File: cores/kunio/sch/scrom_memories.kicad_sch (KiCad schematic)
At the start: 18 parts

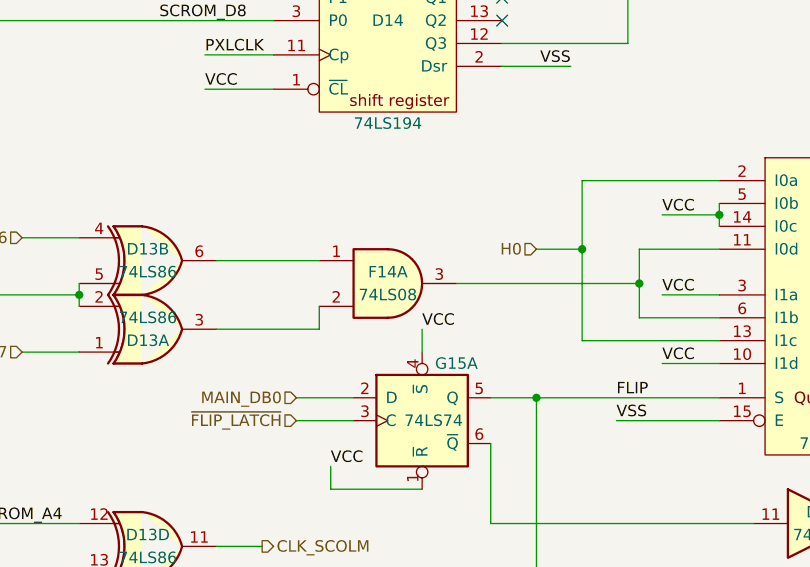
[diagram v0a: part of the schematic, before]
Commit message: update kicad7
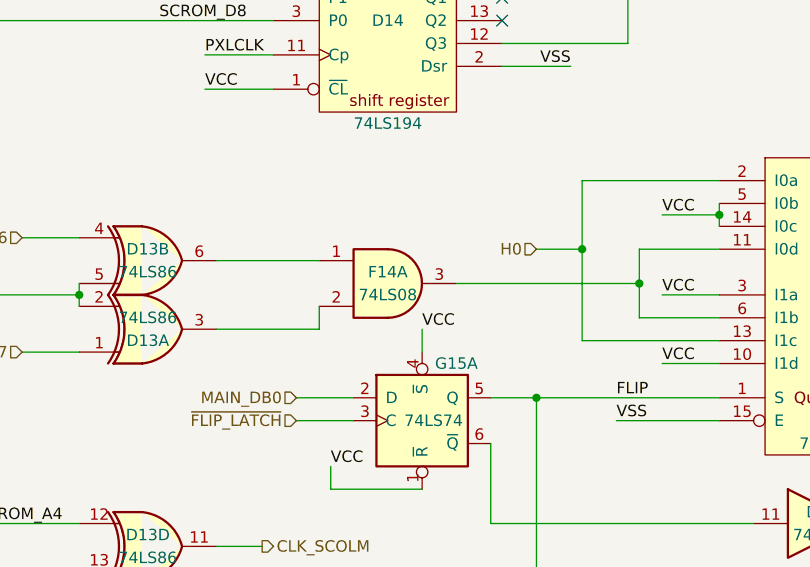
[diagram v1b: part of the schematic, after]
